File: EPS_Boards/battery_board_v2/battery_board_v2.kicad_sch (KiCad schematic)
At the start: 14 parts, among them J1 PC104_Connector

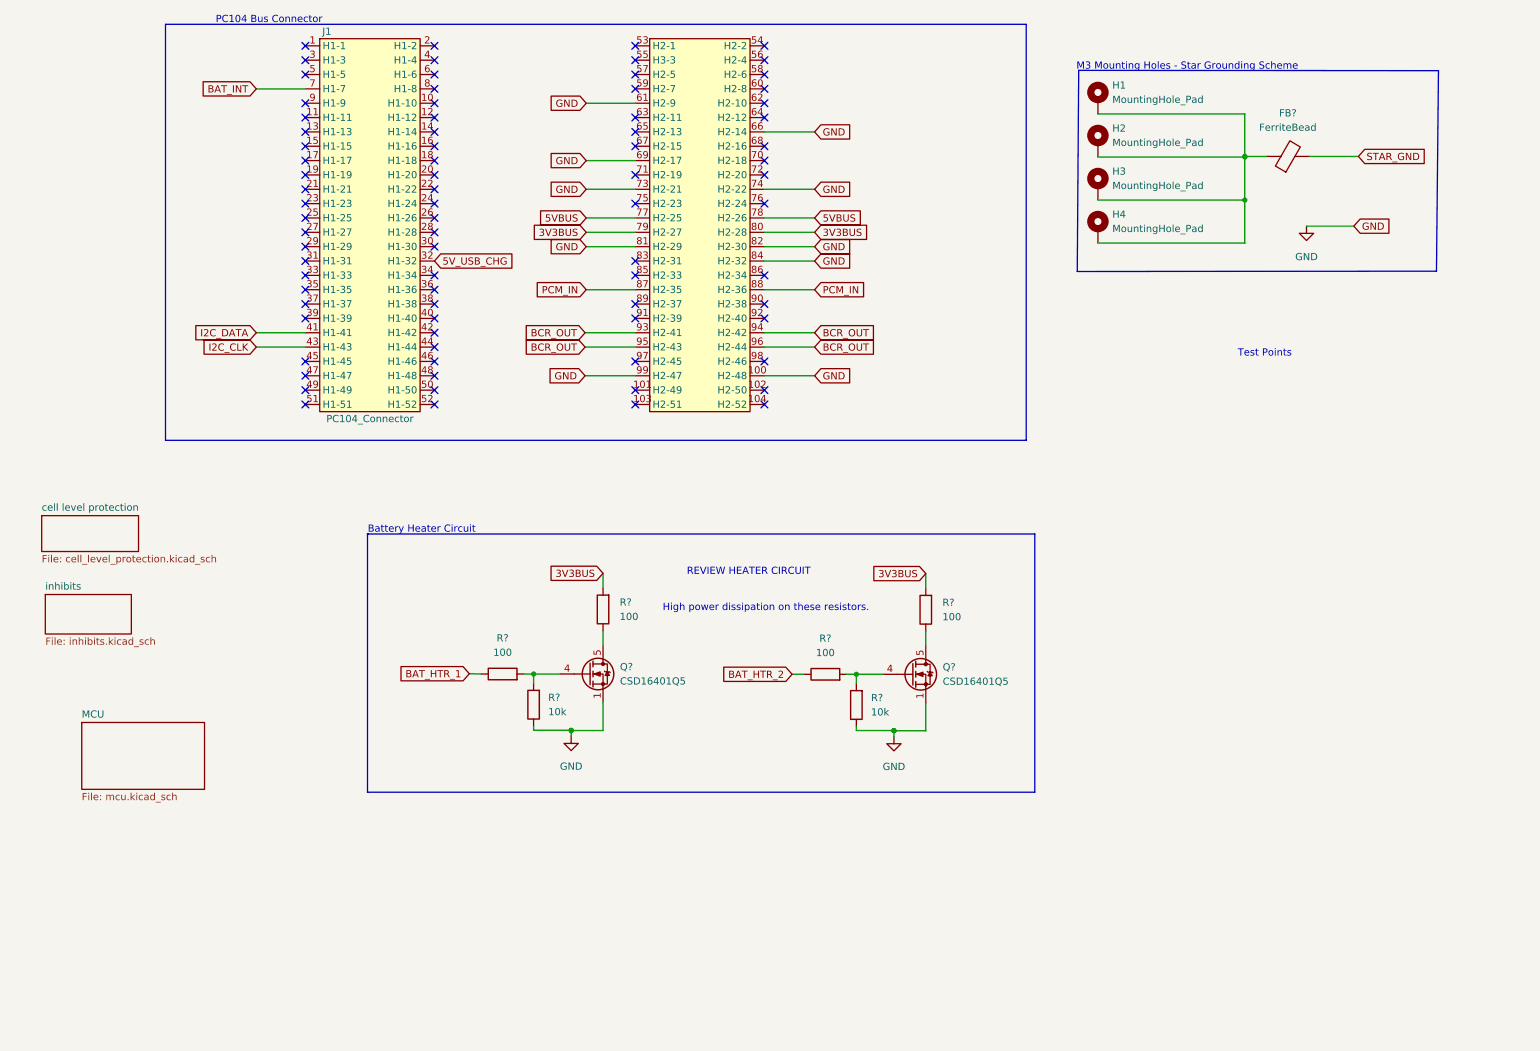
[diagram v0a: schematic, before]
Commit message: eps: battery board: updated schematic
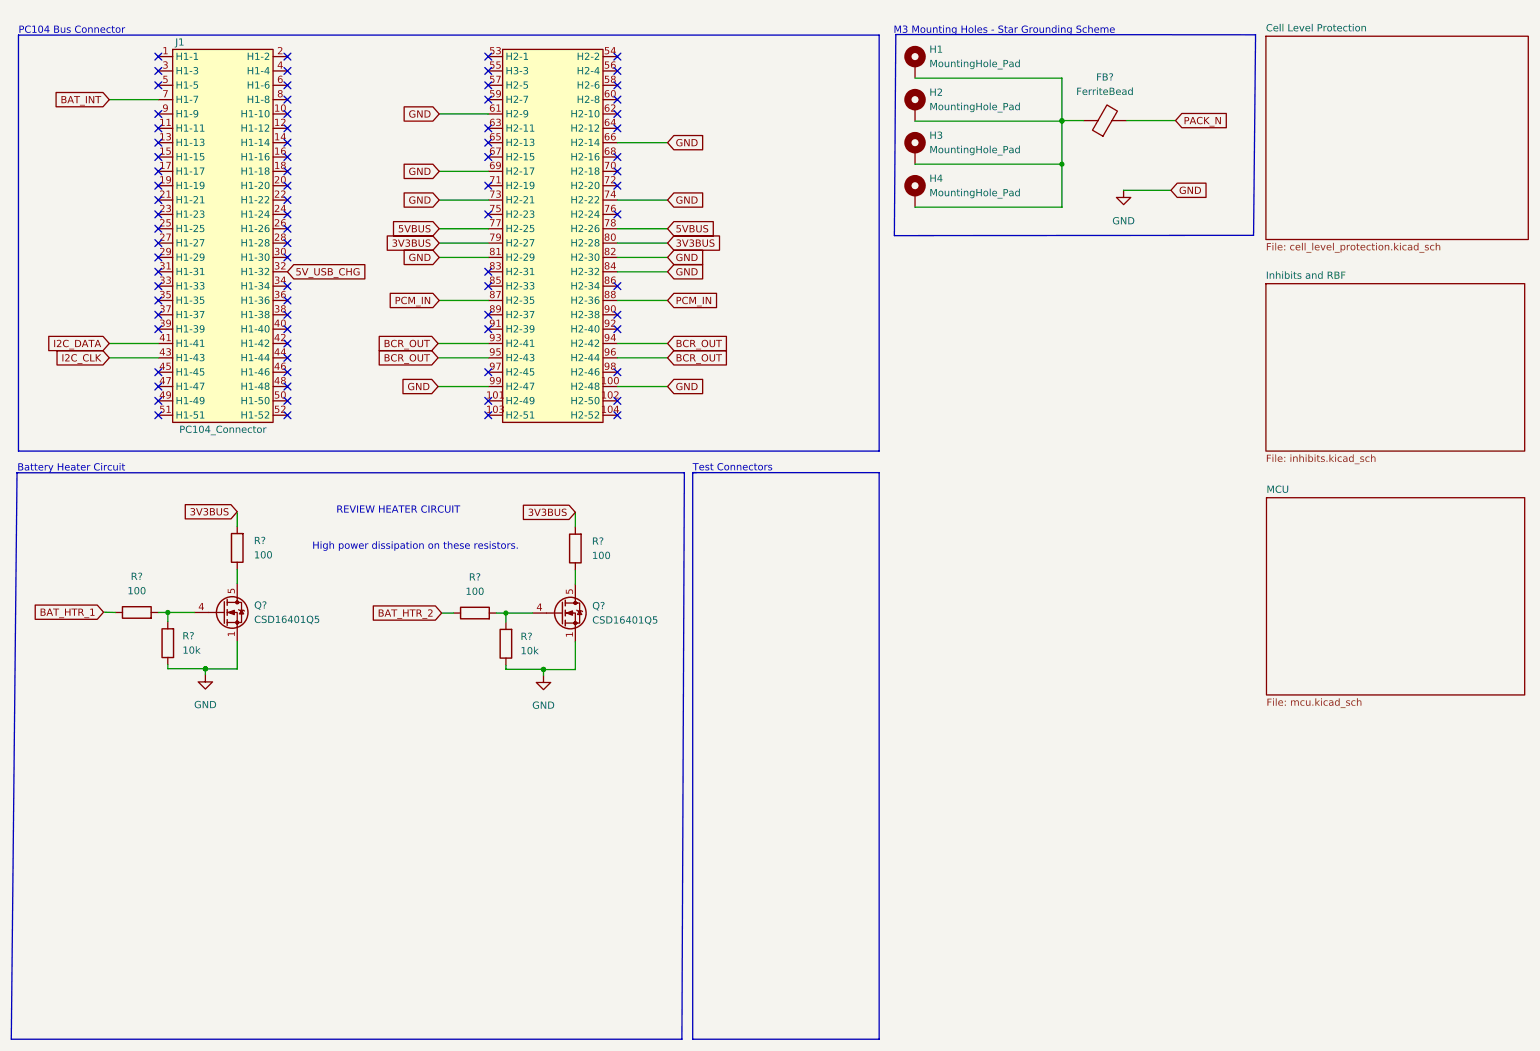
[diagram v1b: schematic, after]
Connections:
- net STAR_GND renamed PACK_N
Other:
- sheet cell level protection renamed Cell Level Protection
- sheet inhibits renamed Inhibits and RBF
- note added: "Test Connectors"
- note removed: "Test Points"
- moved on the sheet: FB?, H1, H2, H3, H4, J1, Q?, R?

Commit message: eps: battery board: added current and voltage monitor
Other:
- added sheet voltage and current monitor (VI_monitor.kicad_sch)
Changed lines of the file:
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@@
+    )
+  )
+  (sheet (at 236.855 142.24) (size 45.72 20.32) (fields_autoplaced)
+    (stroke (width 0.1524) (type solid) (color 0 0 0 0))
+    (fill (color 0 0 0 0.0000))
+    (property "Sheet name" "voltage and current monitor" (id 0) (at 236.855 141.5284 0)
+      (effects (font (size 1.27 1.27)) (justify left bottom))
+    )
+    (property "Sheet file" "VI_monitor.kicad_sch" (id 1) (at 236.855 163.1446 0)
+      (effects (font (size 1.27 1.27)) (justify left top))
     )
   )
@@
     (path "/a4d1c6d9-340c-4b33-a3db-bb415a05c09a" (page "3"))
     (path "/e6e611eb-ef07-4f1d-b587-00ae2ef44ad9" (page "4"))
+    (path "/2bb4228a-f328-4583-9040-951e63b787f8" (page "5"))
   )
   (symbol_instances
@@
       (reference "#PWR?") (unit 1) (value "+3V3") (footprint "")
     )
+    (path "/2bb4228a-f328-4583-9040-951e63b787f8/592a443d-b2d9-439f-8edc-7417ea99004d"
+      (reference "#PWR?") (unit 1) (value "GND") (footprint "")
+    )
+    (path "/2bb4228a-f328-4583-9040-951e63b787f8/6ef8ed37-8f40-437f-b5f0-353b3a1df437"
+      (reference "#PWR?") (unit 1) (value "GND") (footprint "")
+    )
     (path "/22fae705-7a56-4499-bfd1-79d4966b69d0/6efc7701-4952-4804-84f0-976e06042517"
       (reference "#PWR?") (unit 1) (value "GND") (footprint "")
@@
     (path "/22fae705-7a56-4499-bfd1-79d4966b69d0/f0a46a16-cb08-4fae-8e4b-58c476a0ae07"
       (reference "#PWR?") (unit 1) (value "GND") (footprint "")
+    )
+    (path "/2bb4228a-f328-4583-9040-951e63b787f8/f2676342-8596-49be-90f6-be5cf45b7aae"
+      (reference "#PWR?") (unit 1) (value "+3V3") (footprint "")
     )
     (path "/22fae705-7a56-4499-bfd1-79d4966b69d0/ffce51ed-2ae1-4200-b3b9-90a457df2bad"
@@
       (reference "C?") (unit 1) (value "100n") (footprint "Capacitor_SMD:C_0603_1608Metric")
     )
+    (path "/2bb4228a-f328-4583-9040-951e63b787f8/99e89642-4019-492d-8a3c-4d5a2f624193"
+      (reference "C?") (unit 1) (value "0.1u") (footprint "")
+    )
     (path "/22fae705-7a56-4499-bfd1-79d4966b69d0/a5602131-391f-4b8f-850f-36e3e1bf4ac7"
       (reference "C?") (unit 1) (value "10u") (footprint "Capacitor_SMD:C_0603_1608Metric")
@@
       (reference "R?") (unit 1) (value "2.2k") (footprint "")
     )
+    (path "/2bb4228a-f328-4583-9040-951e63b787f8/16f9c22e-1477-460a-907b-b031fb81d944"
+      (reference "R?") (unit 1) (value "0.1") (footprint "")
+    )
     (path "/e6e611eb-ef07-4f1d-b587-00ae2ef44ad9/34ca1c29-8b05-4b4a-b0bd-acaaa58084ac"
       (reference "R?") (unit 1) (value "330") (footprint "")
+    )
+    (path "/2bb4228a-f328-4583-9040-951e63b787f8/3ee91e81-beed-45c4-a9f8-a09d1764ef1b"
+      (reference "R?") (unit 1) (value "3.3k") (footprint "")
     )
     (path "/e6e611eb-ef07-4f1d-b587-00ae2ef44ad9/5e7062cc-01c6-4461-8825-09d0578d1710"
@@
       (reference "R?") (unit 1) (value "10k") (footprint "")
     )
+    (path "/2bb4228a-f328-4583-9040-951e63b787f8/62be2f21-af73-488c-82c1-fa94ec2fd5e4"
+      (reference "R?") (unit 1) (value "3.3k") (footprint "")
+    )
     (path "/e6e611eb-ef07-4f1d-b587-00ae2ef44ad9/772bd99c-7054-4504-a133-9af3e7898507"
       (reference "R?") (unit 1) (value "2.2k") (footprint "")
@@
       (reference "U?") (unit 1) (value "BQ297xx") (footprint "Package_SON:WSON-6_1.5x1.5mm_P0.5mm")
     )
+    (path "/2bb4228a-f328-4583-9040-951e63b787f8/6f57badf-c031-47ef-9732-f35245844ce8"
+      (reference "U?") (unit 1) (value "INA219AxD") (footprint "Package_SO:SOIC-8_3.9x4.9mm_P1.27mm")
+    )
     (path "/e6e611eb-ef07-4f1d-b587-00ae2ef44ad9/97c73686-483e-4c4d-bc95-47bf35a09036"

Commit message: eps: battery board: power control
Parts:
- added Q?: NTJD1155LT1G, TRANS_NTJD1155LT1G, symbol NTJD1155LT1G:NTJD1155LT1G
- added R?: 10k, symbol Device:R
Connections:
- net GND: now also Q?.1, Q?.2
- new net: Q?.6, R?.2
- new net EN_3V3: Q?.5
- new net PACK_NEG: Q?.4, R?.1
- no-connect marks 80 -> 81
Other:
- sheet Inhibits and RBF renamed Power Control and RBF
- note added: "Low-side inhibit switch v1"

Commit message: eps: battery board: added inhibits
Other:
- added sheet inhibits (inhibits2.kicad_sch)
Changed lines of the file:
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@@
+    )
+  )
+  (sheet (at 175.26 60.96) (size 53.34 30.48) (fields_autoplaced)
+    (stroke (width 0.1524) (type solid) (color 0 0 0 0))
+    (fill (color 0 0 0 0.0000))
+    (property "Sheet name" "inhibits" (id 0) (at 175.26 60.2484 0)
+      (effects (font (size 1.27 1.27)) (justify left bottom))
+    )
+    (property "Sheet file" "inhibits2.kicad_sch" (id 1) (at 175.26 92.0246 0)
+      (effects (font (size 1.27 1.27)) (justify left top))
     )
   )
@@
     (path "/e6e611eb-ef07-4f1d-b587-00ae2ef44ad9" (page "4"))
     (path "/2bb4228a-f328-4583-9040-951e63b787f8" (page "5"))
+    (path "/f0f1db07-72ef-4281-870a-8689add45a3e" (page "6"))
   )
   (symbol_instances
@@
       (reference "#PWR?") (unit 1) (value "GND") (footprint "")
     )
+    (path "/f0f1db07-72ef-4281-870a-8689add45a3e/36ba95ac-30f0-493d-8622-2f4ff805b515"
+      (reference "#PWR?") (unit 1) (value "GND") (footprint "")
+    )
     (path "/22fae705-7a56-4499-bfd1-79d4966b69d0/4f6c7b5b-9c6d-4c9a-80b7-81385d3c4dd6"
       (reference "#PWR?") (unit 1) (value "+3V3") (footprint "")
@@
       (reference "C?") (unit 1) (value "0.1u") (footprint "")
     )
+    (path "/f0f1db07-72ef-4281-870a-8689add45a3e/a07ff673-77f5-44c2-9576-c6a6d1c7e494"
+      (reference "C?") (unit 1) (value "22n") (footprint "")
+    )
     (path "/22fae705-7a56-4499-bfd1-79d4966b69d0/a5602131-391f-4b8f-850f-36e3e1bf4ac7"
       (reference "C?") (unit 1) (value "10u") (footprint "Capacitor_SMD:C_0603_1608Metric")
     )
+    (path "/f0f1db07-72ef-4281-870a-8689add45a3e/b2bd229c-51f8-40b6-81a2-2aa43235a60d"
+      (reference "C?") (unit 1) (value "0.1u") (footprint "")
+    )
     (path "/e6e611eb-ef07-4f1d-b587-00ae2ef44ad9/c84d26c8-aeba-4d70-870f-3828eb65ede6"
       (reference "C?") (unit 1) (value "0.1u") (footprint "")
@@
       (reference "Q?") (unit 1) (value "NTJD1155LT1G") (footprint "TRANS_NTJD1155LT1G")
     )
+    (path "/f0f1db07-72ef-4281-870a-8689add45a3e/e0323a1a-378f-4c0e-a91a-57c21b323b96"
+      (reference "Q?") (unit 1) (value "NTJD1155LT1G") (footprint "TRANS_NTJD1155LT1G")
+    )
     (path "/e6e611eb-ef07-4f1d-b587-00ae2ef44ad9/e9e3afea-557c-4bba-adfe-80bb66bca200"
       (reference "Q?") (unit 1) (value "CSD16401Q5") (footprint "Package_TO_SOT_SMD:TDSON-8-1")
@@
       (reference "R?") (unit 1) (value "0R") (footprint "")
     )
+    (path "/f0f1db07-72ef-4281-870a-8689add45a3e/0281611e-a816-407b-ad1b-6433ea68f4f9"
+      (reference "R?") (unit 1) (value "10k") (footprint "")
+    )
     (path "/e6e611eb-ef07-4f1d-b587-00ae2ef44ad9/0ac68cde-e078-493b-a7f0-a2b0a183a6b6"
       (reference "R?") (unit 1) (value "2.2k") (footprint "")
@@
       (reference "R?") (unit 1) (value "2.2k") (footprint "")
     )
+    (path "/f0f1db07-72ef-4281-870a-8689add45a3e/77f6ede2-a895-4d47-b215-4e81b940b0e1"
+      (reference "R?") (unit 1) (value "1k") (footprint "")
+    )
     (path "/7b213a22-9560-4490-afb0-656689cf3445"
       (reference "R?") (unit 1) (value "100") (footprint "")
@@
       (reference "U?") (unit 1) (value "BQ297xx") (footprint "Package_SON:WSON-6_1.5x1.5mm_P0.5mm")
     )
+    (path "/f0f1db07-72ef-4281-870a-8689add45a3e/5bb9d9fa-477f-484f-9ce2-4cdb92d8ef38"
+      (reference "U?") (unit 1) (value "TPS24750") (footprint "")
+    )
     (path "/a4d1c6d9-340c-4b33-a3db-bb415a05c09a/6462c3db-ace9-4885-84b0-fffd92c80453"

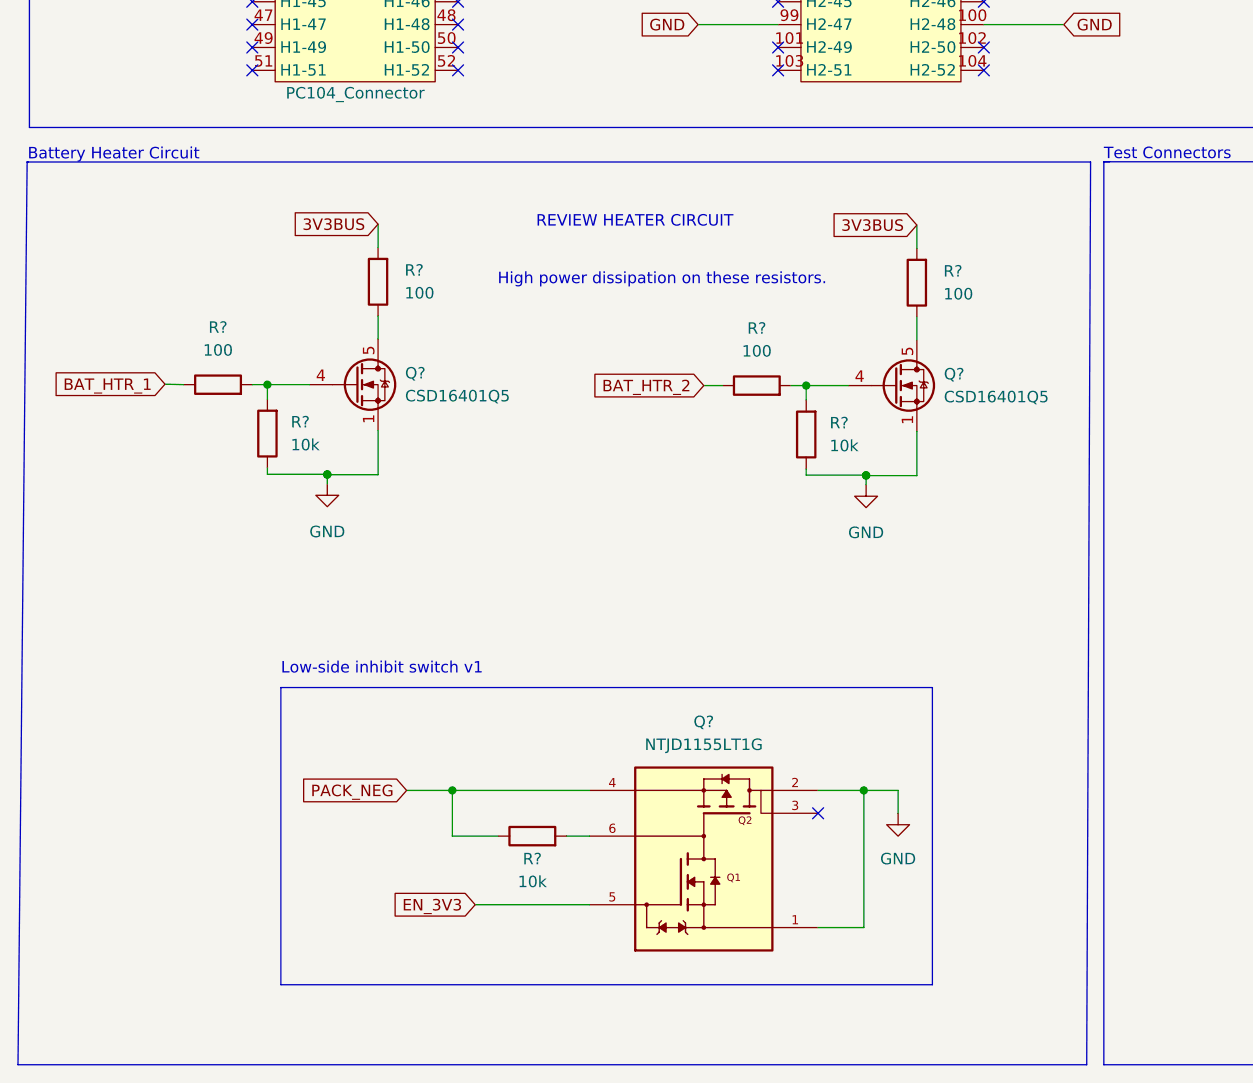
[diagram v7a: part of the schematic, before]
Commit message: eps: battery board: added AND gate for power control and cleaned up global labels
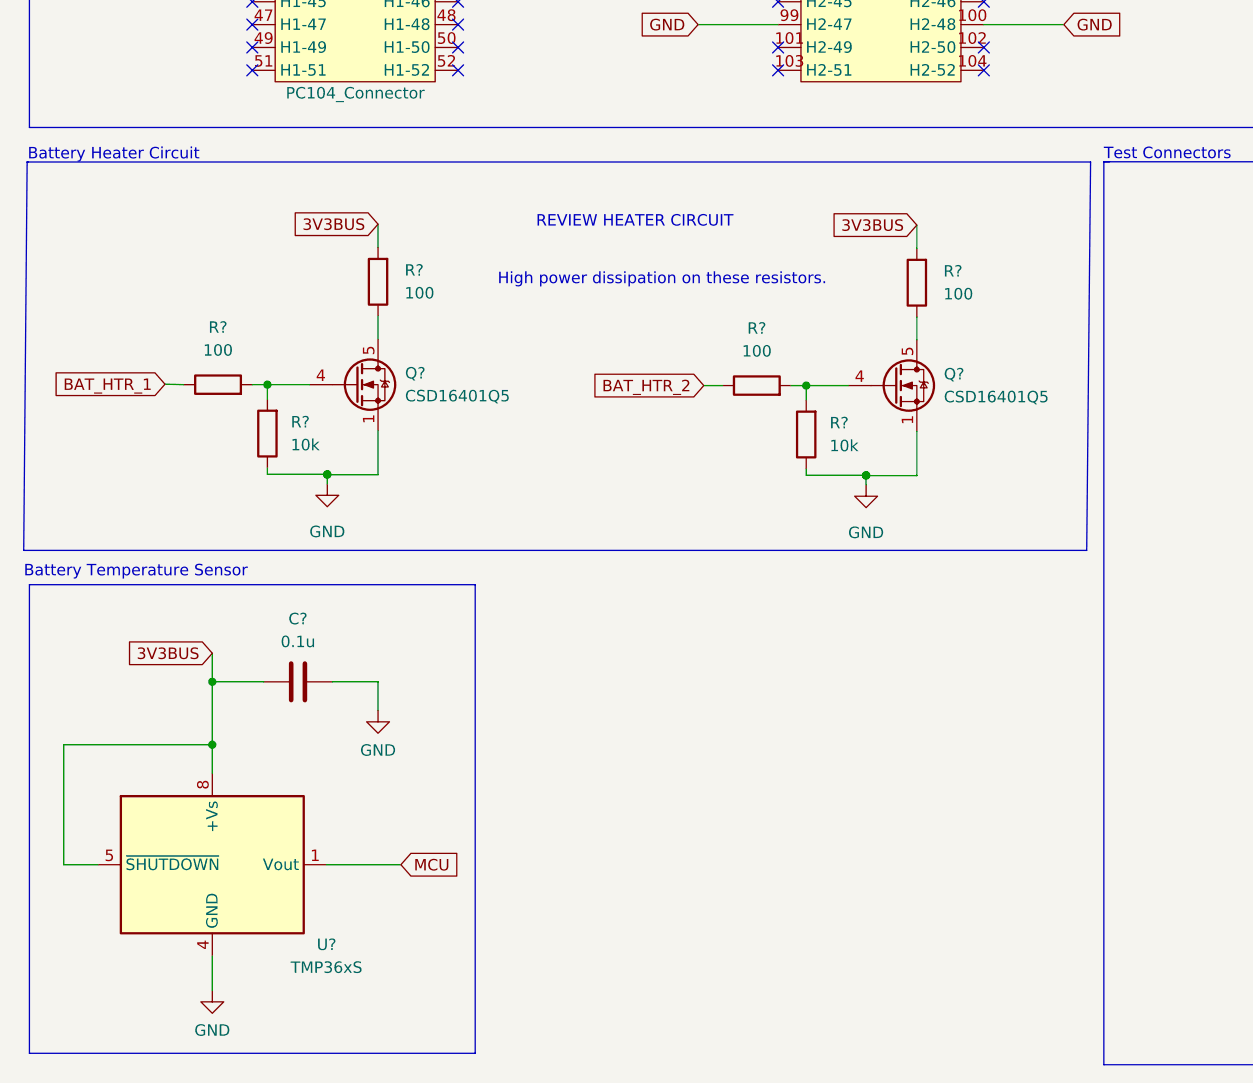
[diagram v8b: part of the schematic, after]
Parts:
- removed Q?: NTJD1155LT1G, TRANS_NTJD1155LT1G, symbol NTJD1155LT1G:NTJD1155LT1G
- removed R?: 10k, symbol Device:R
- added C?: 0.1u, symbol Device:C
- added U?: TMP36xS, Package_SO:SOIC-8_3.9x4.9mm_P1.27mm, symbol Sensor_Temperature:TMP36xS
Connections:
- net 3V3BUS: now also C?.2, U?.5 (~{SHUTDOWN}), U?.8 (+Vs)
- net GND: now also C?.1, U?.4 (GND)
- new net MCU: U?.1 (Vout)
- no-connect marks 81 -> 80
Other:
- note added: "Battery Temperature Sensor"
- note removed: "Low-side inhibit switch v1"
